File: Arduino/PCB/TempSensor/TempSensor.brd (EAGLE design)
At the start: 40.3 x 30.5 mm, 13 parts, among them IC1 DS18B20, U1 ATMEGA328-AU, X1 16Mhz

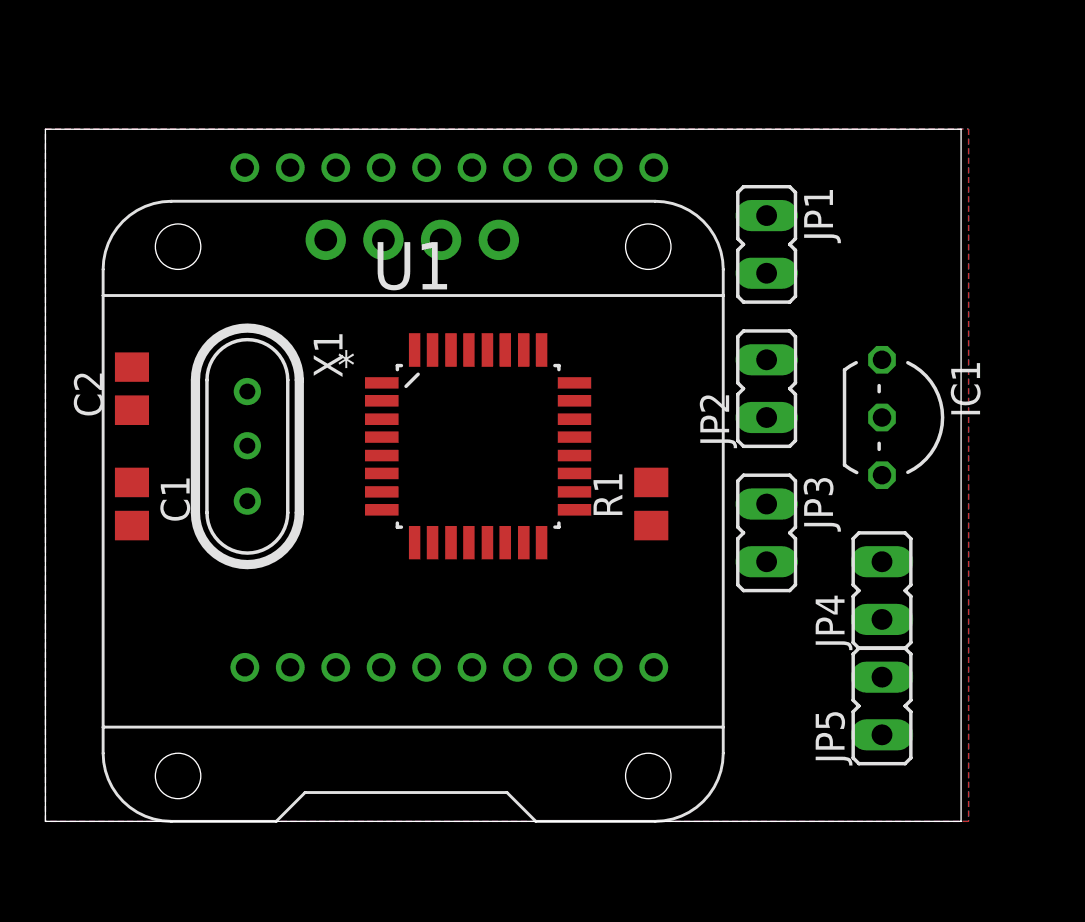
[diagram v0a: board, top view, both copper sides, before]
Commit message: 
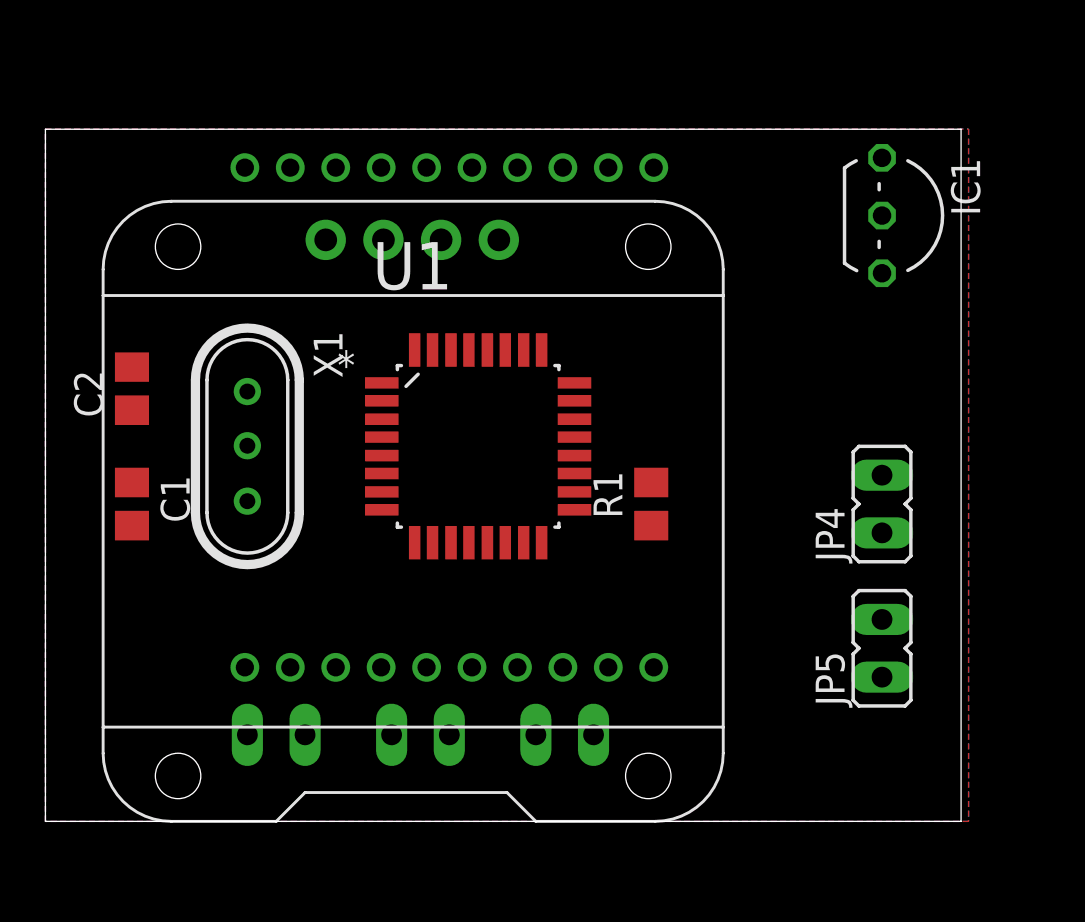
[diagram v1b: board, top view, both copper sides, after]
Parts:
- moved JP1 30.5 mm to (39.4, 25.4), flipped to the bottom, turned to 270 degrees
- moved JP2 21.6 mm to (45.7, 25.4), flipped to the bottom, turned to 90 degrees
- moved JP3 12.6 mm to (52.1, 25.4), flipped to the bottom, turned to 270 degrees
- moved IC1 8.89 mm to (66.0, 48.3)
- moved JP4 3.81 mm to (66.0, 35.6)
- moved JP5 2.54 mm to (66.0, 29.2)

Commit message: sensor pcb
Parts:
- removed JP2, JP3: (no value), jumper:JP1
- added C3: 100n, rcl:C0805
- added J1, J2: FTDI_DEVICE, SparkFun-Connectors:FTDI_DEVICE_SIDE
- added JP6: (no value), jumper:JP1
- added JP7, JP8: (no value), jumper:JP2
- added LED1: 2mA, led:LED3MM
- added R2: 580, rcl:R0603
- added R3: 10k, rcl:R0805
- added SJ2: (no value), jumper:SJ_2
- added U$3: IE0503D, xp_power:XP_DIP
- JP1: device jumper:JP1 -> jumper:JP2
- R1: value (none) -> 4k7
- moved C1 31.1 mm to (63.5, 29.2), flipped to the bottom, turned to 180 degrees
- moved JP5 28.8 mm to (47.0, 50.8), flipped to the bottom, turned to 90 degrees
- moved JP4 28.5 mm to (41.9, 50.8), flipped to the bottom, turned to 90 degrees
- moved C2 23.3 mm to (53.3, 29.2), flipped to the bottom, turned to 180 degrees
- moved X1 22.2 mm to (58.4, 29.2), turned to 0 degrees
- moved XB1 11.4 mm to (57.1, 34.3), turned to 0 degrees
- moved U$2 10.2 mm to (55.9, 35.6)
- moved U1 8.89 mm to (57.1, 38.1), turned to 90 degrees
- moved R1 6.48 mm to (49.5, 36.8), turned to 270 degrees
- moved JP1 5.68 mm to (36.8, 30.5), flipped to the top, turned to 180 degrees
- moved IC1 2.84 mm to (64.8, 50.8), turned to 0 degrees
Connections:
- removed net N$3: JP3.2, XB1.1
- new net +5V: J1.P$4, JP1.1
- new net N$11: JP6.2, U$3.+VIN
- new net N$14: JP6.1, U$3.-VIN
- new net N$15: LED1.K, R2.2
- new net N$16: R2.1, U1.10
- new net N$17: SJ2.2, U1.11
- new net N$18: JP7.3, XB1.2
- new net N$19: JP8.3, XB1.3
- new net N$20: C3.1, J2.P$4, R3.1, U1.29
- new net N$21: C3.2, J1.P$1
- new net N$22: J2.P$3, U1.15
- new net N$23: J2.P$1, U1.17
- new net N$24: J2.P$2, U1.16
- new net VCC: J2.P$5, JP1.2, LED1.A, SJ2.1, U$2.VCC, U1.18, U1.4, U1.6
- net +3V3: now also JP1.3, R3.2, U$3.+VOUT, XB1.1; no longer JP3.1, U$2.VCC, U1.18, U1.4, U1.6
- net GND: now also J1.P$6, J2.P$6, SJ2.3, U$3.-VOUT
- net N$4: now also JP7.2; no longer JP1.1
- net N$5: now also JP8.2, U1.31; no longer JP1.2, XB1.2
- net N$6: now also J1.P$3, JP7.1; no longer JP2.1, XB1.3
- net N$7: now also J1.P$2, JP8.1; no longer JP2.2, U1.31
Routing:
- net VCC: track 0.00 -> 79.6 mm, vias 0 -> 2
- net +3V3: track 0.00 -> 78.5 mm, vias 0 -> 3
- net N$16: track 0.00 -> 66.4 mm, vias 0 -> 3
- net N$18: track 0.00 -> 63.7 mm, vias 0 -> 3
- net N$19: track 0.00 -> 58.4 mm, vias 0 -> 4
- net N$4: track 0.00 -> 52.0 mm, vias 0 -> 4
- net N$12: track 0.00 -> 34.0 mm, vias 0 -> 3
- net N$5: track 0.00 -> 33.9 mm, vias 0 -> 1
- net N$10: track 0.00 -> 32.8 mm, vias 0 -> 2
- net 1W: track 0.00 -> 30.4 mm, vias 0 -> 2
- net N$23: track 0.00 -> 29.8 mm, vias 0 -> 2
- net N$22: track 0.00 -> 27.7 mm, vias 0 -> 2
- net N$13: track 0.00 -> 26.0 mm, vias 0 -> 2
- net N$24: track 0.00 -> 25.4 mm, vias 0 -> 2
- net N$21: track 0.00 -> 23.2 mm, vias 0 -> 1
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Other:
- board size 40.3 x 30.5 mm -> 37.8 x 31.7 mm

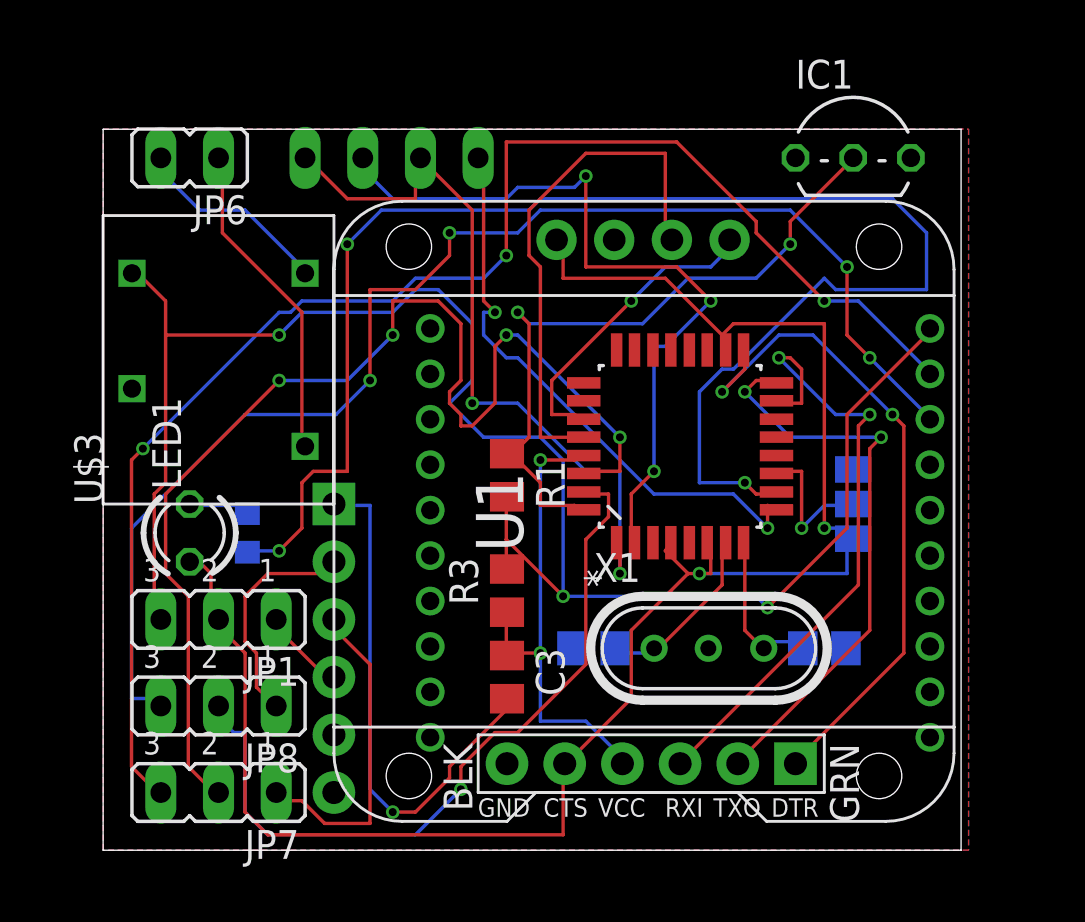
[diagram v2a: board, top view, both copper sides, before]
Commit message: 
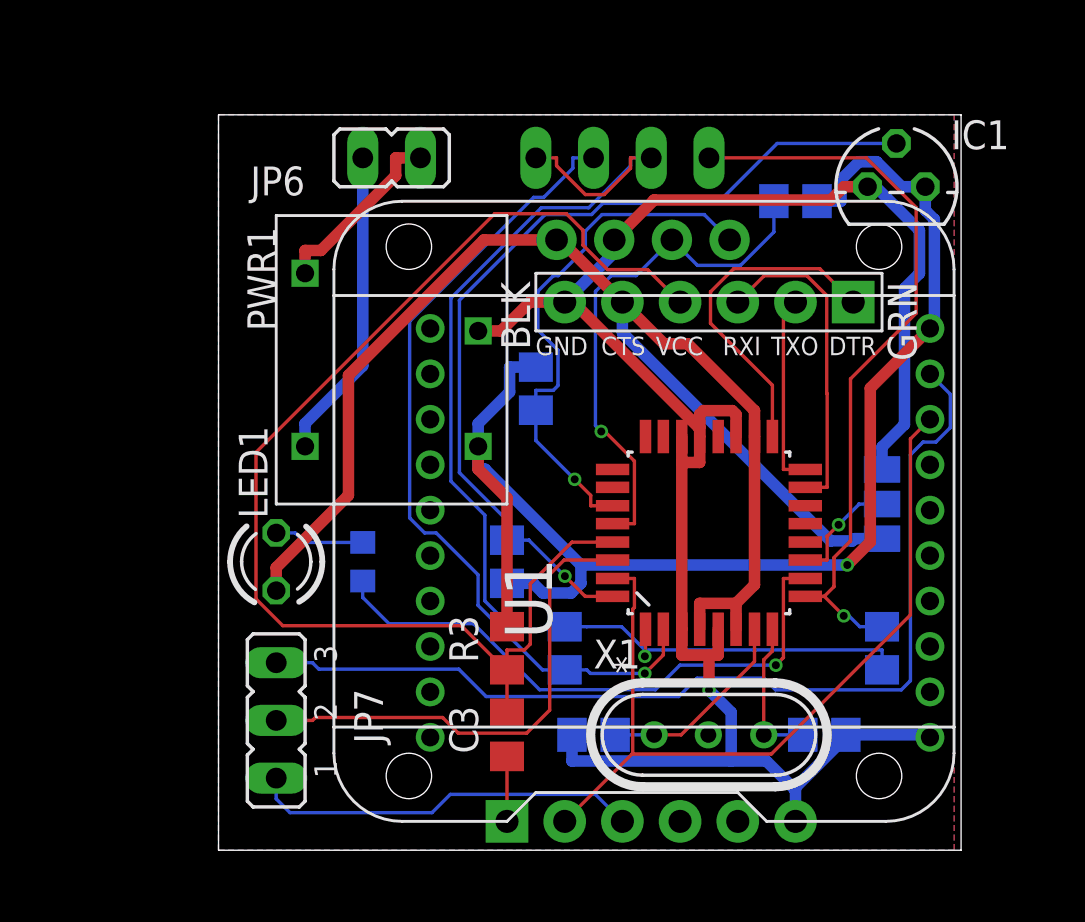
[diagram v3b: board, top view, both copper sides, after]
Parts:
- removed JP1, JP8: (no value), jumper:JP2
- removed U$3: IE0503D, xp_power:XP_DIP
- added PWR1: IE0503D, xp_power:XP_DIP
- added R4, R5, R6, R7: 4k7, rcl:R0805
- IC1: value DS18B20 -> DS1820; device 1wire:TO92- -> DS1820:TO-92
- moved J2 20.5 mm to (58.4, 44.5)
- moved J1 15.9 mm to (55.9, 21.6), turned to 180 degrees
- moved JP4 10.2 mm to (52.1, 50.8)
- moved JP5 10.2 mm to (57.1, 50.8)
- moved JP6 8.89 mm to (44.5, 50.8)
- moved R2 5.24 mm to (43.2, 33.0)
- moved JP7 4.07 mm to (39.4, 26.0), turned to 90 degrees
- moved U1 4.02 mm to (58.4, 34.3)
- moved LED1 4.02 mm to (39.4, 33.0)
- moved C1 3.81 mm to (63.5, 25.4)
- moved C2 3.81 mm to (53.3, 25.4)
- moved X1 3.81 mm to (58.4, 25.4)
- moved R1 3.81 mm to (49.5, 33.0), flipped to the bottom
- moved C3 2.54 mm to (49.5, 25.4)
- moved R3 2.54 mm to (49.5, 29.2)
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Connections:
- net 1W renamed N$6
- removed net +5V: J1.P$4, JP1.1
- removed net N$19: JP8.3, XB1.3
- removed net N$7: J1.P$2, JP8.1
- removed net VDD: IC1.3
- net +3V3: now also IC1.3, PWR1.+VOUT, R4.2, R5.2; no longer JP1.3, U$3.+VOUT
- net GND: now also PWR1.-VOUT; no longer U$3.-VOUT
- net N$10: now also R6.2, R7.2
- net N$11: now also PWR1.+VIN; no longer U$3.+VIN
- net N$12: now also R6.1
- net N$13: now also R7.1
- net N$14: now also PWR1.-VIN; no longer U$3.-VIN
- net N$5: now also J1.P$2, XB1.3; no longer JP8.2
- net N$8: now also R4.1
- net N$9: now also R5.1
- net VCC: no longer JP1.2
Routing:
- net GND: track 0.00 -> 85.6 mm, vias 0 -> 1
- net N$19: track 58.4 -> 0.00 mm, vias 4 -> 0
- net N$16: track 66.4 -> 26.0 mm, vias 3 -> 1
- net N$20: track 21.4 -> 54.6 mm, vias 2 -> 0
- net N$4: track 52.0 -> 21.8 mm, vias 4 -> 0
- net N$10: track 32.8 -> 53.3 mm, vias 2 -> 1
- net N$21: track 23.2 -> 2.86 mm, vias 1 -> 0
- net N$18: track 63.7 -> 44.2 mm, vias 3 -> 0
- net N$24: track 25.4 -> 8.55 mm, vias 2 -> 0
- net +3V3: track 78.5 -> 62.0 mm, vias 3 -> 1
- net VCC: track 79.6 -> 63.6 mm, vias 2 -> 0
- net N$23: track 29.8 -> 14.8 mm, vias 2 -> 0
- net N$22: track 27.7 -> 14.2 mm, vias 2 -> 0
- net N$7: track 10.2 -> 0.00 mm
- net N$8: track 13.7 -> 23.4 mm
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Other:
- board size 37.8 x 31.7 mm -> 32.7 x 32.4 mm
